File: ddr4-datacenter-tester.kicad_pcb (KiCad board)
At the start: 10 copper layers, 152.9 x 90 mm, 288 parts, among them IC1 TPS54561, IC3 TPD8S009DSMR, J1 0878311420, J10 61300311121, J3 DC_SOCKET, J4 WE_629105150521, J6 685119134923, J7 1140084168, J8 61300311121, Q2 BSS138APW, Q3 BSS138APW, Q4 BSS138APW, Q5 BSS138APW, Q6 BSS138APW, Q7 BSS138APW, Q8 BSS138APW, U10 LM3881MME_NOPB, U11 S27KL0641DABHI023, U12 TPS62823DLCT, U14 2199155-1, U15 XC7K160T-FFG676, U2 ASFLMB-100.000MHZ-XY-T, U3 S25FL128SAGNFI000, U4 TPS65296, U5 TPS62823DLCT, U6 KSZ9031RNXCA, U7 FT4232HQ, U8 SRST, U9 TPS62823DLCT, Y1 ABM8G-25.000MHZ-18-D2Y-T, Y2 ABM8G-12.000MHZ-18-D2Y-T

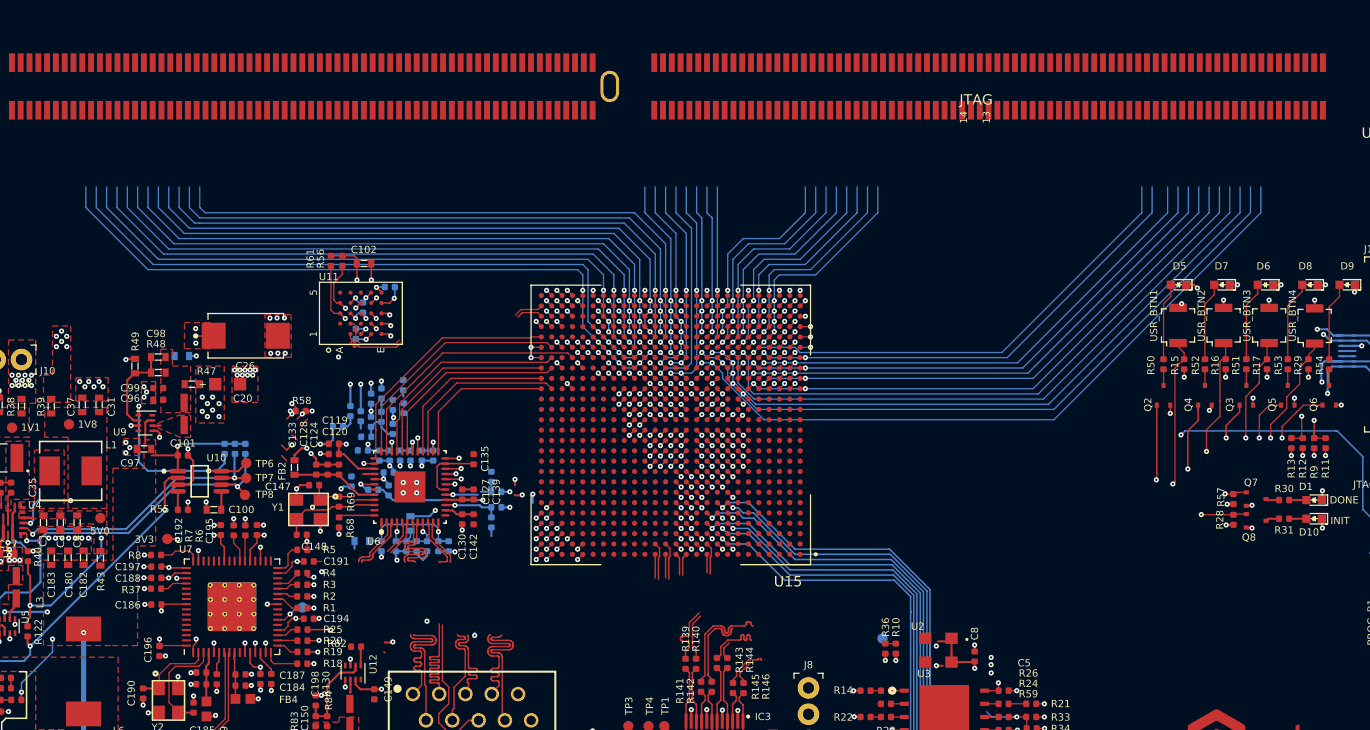
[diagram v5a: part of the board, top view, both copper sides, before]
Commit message: ADD DDR4 connection to FPGA and signals routing - WIP
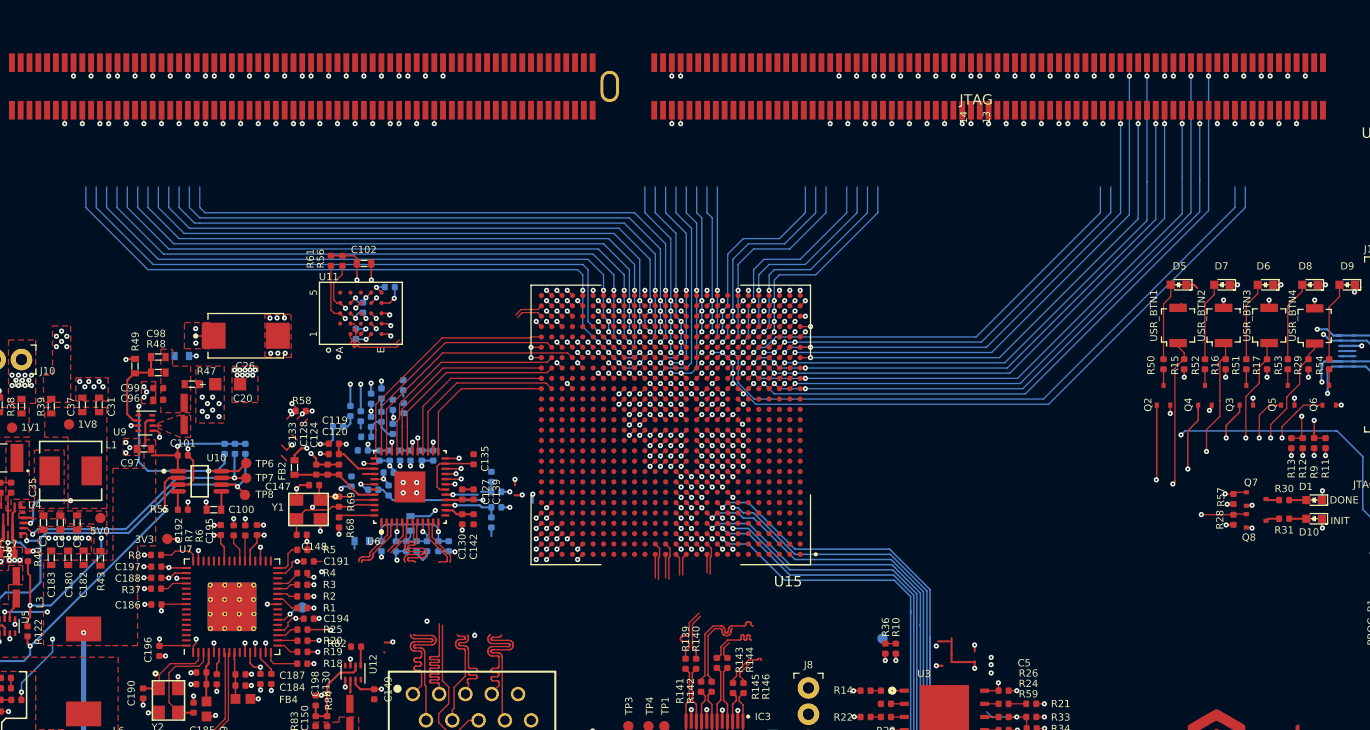
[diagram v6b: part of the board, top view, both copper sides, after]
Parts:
- removed C8: C_100n_0402_6V3, ddr4-datacenter-tester-footprints:0402-cap
- removed U2: ASFLMB-100.000MHZ-XY-T, ddr4-datacenter-tester-footprints:ASFLMB-100.000MHZ-XY-T
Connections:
- net /DDR4/12V renamed 12V
- net /DDR4/A0 renamed A0
- net /DDR4/A1 renamed A1
- net /DDR4/A10\AP renamed A10\AP
- net /DDR4/A11 renamed A11
- net /DDR4/A12\~BC renamed A12\~BC
- net /DDR4/A13 renamed A13
- net /DDR4/A17 renamed A17
- net /DDR4/A2 renamed A2
- net /DDR4/A3 renamed A3
- net /DDR4/A4 renamed A4
- net /DDR4/A5 renamed A5
- net /DDR4/A6 renamed A6
- net /DDR4/A7 renamed A7
- net /DDR4/A8 renamed A8
- net /DDR4/A9 renamed A9
- net /DDR4/BA0 renamed BA0
- net /DDR4/BA1 renamed BA1
- net /DDR4/BG0 renamed BG0
- net /DDR4/BG1 renamed BG1
- net /DDR4/CKE0 renamed CKE0
- net /DDR4/CKE1\NC renamed CKE1\NC
- net /DDR4/DQ32 renamed DQ32
- net /DDR4/DQ33 renamed DQ33
- net /DDR4/DQ34 renamed DQ34
- net /DDR4/DQ35 renamed DQ35
- net /DDR4/DQ36 renamed DQ36
- net /DDR4/DQ37 renamed DQ37
- net /DDR4/DQ38 renamed DQ38
- net /DDR4/DQ39 renamed DQ39
- net /DDR4/DQ40 renamed DQ40
- net /DDR4/DQ41 renamed DQ41
- net /DDR4/DQ42 renamed DQ42
- net /DDR4/DQ43 renamed DQ43
- net /DDR4/DQ44 renamed DQ44
- net /DDR4/DQ45 renamed DQ45
- net /DDR4/DQ46 renamed DQ46
- net /DDR4/DQ47 renamed DQ47
- net /DDR4/DQ48 renamed DQ48
- net /DDR4/DQ49 renamed DQ49
- net /DDR4/DQ50 renamed DQ50
- net /DDR4/DQ51 renamed DQ51
- net /DDR4/DQ52 renamed DQ52
- net /DDR4/DQ53 renamed DQ53
- net /DDR4/DQ54 renamed DQ54
- net /DDR4/DQ55 renamed DQ55
- net /DDR4/DQ56 renamed DQ56
- net /DDR4/DQ57 renamed DQ57
- net /DDR4/DQ58 renamed DQ58
- net /DDR4/DQ59 renamed DQ59
- net /DDR4/DQ60 renamed DQ60
- net /DDR4/DQ61 renamed DQ61
- net /DDR4/DQ62 renamed DQ62
- net /DDR4/DQ63 renamed DQ63
- net /DDR4/DQS11_C renamed DQS11_C
- net /DDR4/DQS11_T renamed DQS11_T
- net /DDR4/DQS12_C renamed DQS12_C
- net /DDR4/DQS12_T renamed DQS12_T
- net /DDR4/DQS13_C renamed DQS13_C
- net /DDR4/DQS13_T renamed DQS13_T
- net /DDR4/DQS14_C renamed DQS14_C
- net /DDR4/DQS14_T renamed DQS14_T
- net /DDR4/DQS15_C renamed DQS15_C
- net /DDR4/DQS15_T renamed DQS15_T
- net /DDR4/DQS16_C renamed DQS16_C
- net /DDR4/DQS16_T renamed DQS16_T
- net /DDR4/DQS17_C renamed DQS17_C
- net /DDR4/DQS17_T renamed DQS17_T
- net /DDR4/DQS4_C renamed DQS4_C
- net /DDR4/DQS4_T renamed DQS4_T
- net /DDR4/DQS5_C renamed DQS5_C
- net /DDR4/DQS5_T renamed DQS5_T
- net /DDR4/DQS6_C renamed DQS6_C
- net /DDR4/DQS6_T renamed DQS6_T
- net /DDR4/DQS7_C renamed DQS7_C
- net /DDR4/DQS7_T renamed DQS7_T
- net /DDR4/DQS9_C renamed DQS9_C
- net /DDR4/DQS9_T renamed DQS9_T
- net /DDR4/NC\C2 renamed NC\C2
- net /DDR4/ODT0 renamed ODT0
- net /DDR4/ODT1\NC renamed ODT1\NC
- net /DDR4/PARITY renamed PARITY
- net /DDR4/SA0 renamed SA0
- net /DDR4/SA1 renamed SA1
- net /DDR4/SA2 renamed SA2
- net /DDR4/SCL renamed SCL
- net /DDR4/SDA renamed SDA
- net /DDR4/~ACT renamed ~ACT
- net /DDR4/~ALERT renamed ~ALERT
- net /DDR4/~CAS~\A15 renamed ~CAS~\A15
- net /DDR4/~CS0 renamed ~CS0
- net /DDR4/~CS1~\NC renamed ~CS1~\NC
- net /DDR4/~CS2~\C0 renamed ~CS2~\C0
- net /DDR4/~CS3~\C1,NC renamed ~CS3~\C1,NC
- net /DDR4/~EVENT renamed ~EVENT
- net /DDR4/~RAS~\A16 renamed ~RAS~\A16
- net /DDR4/~RESET renamed ~RESET
- net /DDR4/~SAVE renamed ~SAVE
- net /DDR4/~WE~\A14 renamed ~WE~\A14
- U14 pad 10: /DDR4/DQ6 -> DQ6
- U14 pad 12: /DDR4/DQ2 -> DQ2
- U14 pad 14: /DDR4/DQ12 -> DQ12
- U14 pad 148: /DDR4/DQ5 -> DQ5
- U14 pad 150: /DDR4/DQ1 -> DQ1
- U14 pad 152: /DDR4/DQS10_C -> DQS0_C
- U14 pad 153: /DDR4/DQS10_T -> DQS0_T
- U14 pad 155: /DDR4/DQ7 -> DQ7
- U14 pad 157: /DDR4/DQ3 -> DQ3
- U14 pad 159: /DDR4/DQ13 -> DQ13
- U14 pad 16: /DDR4/DQ8 -> DQ8
- U14 pad 161: /DDR4/DQ9 -> DQ9
- U14 pad 163: /DDR4/DQS1_C -> DQS1_C
- U14 pad 164: /DDR4/DQS1_T -> DQS1_T
- U14 pad 166: /DDR4/DQ15 -> DQ15
- U14 pad 168: /DDR4/DQ11 -> DQ11
- U14 pad 170: /DDR4/DQ21 -> DQ21
- U14 pad 172: /DDR4/DQ17 -> DQ17
- U14 pad 174: /DDR4/DQS2_C -> DQS2_C
- U14 pad 175: /DDR4/DQS2_T -> DQS2_T
- U14 pad 177: /DDR4/DQ23 -> DQ23
- U14 pad 179: /DDR4/DQ19 -> DQ19
- U14 pad 18: /DDR4/DQS10_T -> DQS10_T
- U14 pad 181: /DDR4/DQ29 -> DQ29
- U14 pad 183: /DDR4/DQ25 -> DQ25
- U14 pad 185: /DDR4/DQS3_C -> DQS3_C
- U14 pad 186: /DDR4/DQS3_T -> DQS3_T
- U14 pad 188: /DDR4/DQ31 -> DQ31
- U14 pad 19: /DDR4/DQS10_C -> DQS10_C
- U14 pad 190: /DDR4/DQ27 -> DQ27
- U14 pad 192: /DDR4/CB5 -> CB5
- U14 pad 194: /DDR4/CB1 -> CB1
- U14 pad 196: /DDR4/DQS8_C -> DQS8_C
- U14 pad 197: /DDR4/DQS8_T -> DQS8_T
- U14 pad 199: /DDR4/CB7 -> CB7
- U14 pad 201: /DDR4/CB3 -> CB3
- U14 pad 21: /DDR4/DQ14 -> DQ14
- U14 pad 218: /DDR4/CK1_T -> CK1_T
- U14 pad 219: /DDR4/CK1_C -> CK1_C
- U14 pad 23: /DDR4/DQ10 -> DQ10
- U14 pad 25: /DDR4/DQ20 -> DQ20
- U14 pad 27: /DDR4/DQ16 -> DQ16
- U14 pad 3: /DDR4/DQ4 -> DQ4
- U14 pad 32: /DDR4/DQ22 -> DQ22
- U14 pad 34: /DDR4/DQ18 -> DQ18
- U14 pad 36: /DDR4/DQ28 -> DQ28
- U14 pad 38: /DDR4/DQ24 -> DQ24
- U14 pad 43: /DDR4/DQ30 -> DQ30
- U14 pad 45: /DDR4/DQ26 -> DQ26
- U14 pad 47: /DDR4/CB4 -> CB4
- U14 pad 49: /DDR4/CB0 -> CB0
- U14 pad 5: /DDR4/DQ0 -> DQ0
- U14 pad 54: /DDR4/CB6 -> CB6
- U14 pad 56: /DDR4/CB2 -> CB2
- U14 pad 74: /DDR4/CK0_T -> CK0_T
- U14 pad 75: /DDR4/CK0_C -> CK0_C
- U15 pad AA2: Net-(U15-PadAA2) -> DQ16
- U15 pad AB1: Net-(U15-PadAB1) -> DQS2_T
- U15 pad AB12: Net-(U15-PadAB12) -> CK1_C
- U15 pad AB2: Net-(U15-PadAB2) -> DQ17
- U15 pad AB7: Net-(U15-PadAB7) -> DQ28
- U15 pad AC1: Net-(U15-PadAC1) -> DQS2_C
- U15 pad AC11: Net-(U15-PadAC11) -> DQ27
- U15 pad AC12: Net-(U15-PadAC12) -> CK1_T
- U15 pad AC2: Net-(U15-PadAC2) -> DQ23
- U15 pad AC6: Net-(U15-PadAC6) -> CB3
- U15 pad AC7: Net-(U15-PadAC7) -> DQ29
- U15 pad AC8: Net-(U15-PadAC8) -> DQS3_T
- U15 pad AC9: Net-(U15-PadAC9) -> DQ31
- U15 pad AD1: Net-(U15-PadAD1) -> DQ22
- U15 pad AD10: Net-(U15-PadAD10) -> DQ26
- U15 pad AD5: Net-(U15-PadAD5) -> CB7
- U15 pad AD6: Net-(U15-PadAD6) -> CB2
- U15 pad AD8: Net-(U15-PadAD8) -> DQS3_C
- U15 pad AD9: Net-(U15-PadAD9) -> DQ30
- U15 pad AE1: Net-(U15-PadAE1) -> DQ18
- U15 pad AE12: Net-(U15-PadAE12) -> CK0_T
- U15 pad AE2: Net-(U15-PadAE2) -> DQ19
- U15 pad AE3: Net-(U15-PadAE3) -> CB5
- U15 pad AE5: Net-(U15-PadAE5) -> CB1
- U15 pad AE6: Net-(U15-PadAE6) -> CB6
- U15 pad AE7: Net-(U15-PadAE7) -> DQ24
- U15 pad AF12: Net-(U15-PadAF12) -> CK0_C
- U15 pad AF2: Net-(U15-PadAF2) -> CB4
- U15 pad AF3: Net-(U15-PadAF3) -> CB0
- U15 pad AF4: Net-(U15-PadAF4) -> DQS8_C
- U15 pad AF5: Net-(U15-PadAF5) -> DQS8_T
- U15 pad AF7: Net-(U15-PadAF7) -> DQ25
- U15 pad C15: 3V3_SYS -> Net-(U15-PadC15)
- U15 pad U2: Net-(U15-PadU2) -> DQ8
- U15 pad U4: Net-(U15-PadU4) -> DQ13
- U15 pad U5: Net-(U15-PadU5) -> DQ12
- U15 pad V11: Net-(U15-PadV11) -> DQ4
- U15 pad V2: Net-(U15-PadV2) -> DQ20
- U15 pad V6: Net-(U15-PadV6) -> DQ9
- U15 pad V7: Net-(U15-PadV7) -> DQ2
- U15 pad V8: Net-(U15-PadV8) -> DQ6
- U15 pad V9: Net-(U15-PadV9) -> DQ5
- U15 pad W1: Net-(U15-PadW1) -> DQ21
- U15 pad W10: Net-(U15-PadW10) -> DQS0_T
- U15 pad W11: Net-(U15-PadW11) -> DQ0
- U15 pad W3: Net-(U15-PadW3) -> DQ14
- U15 pad W5: Net-(U15-PadW5) -> DQS1_C
- U15 pad W6: Net-(U15-PadW6) -> DQS1_T
- U15 pad W8: Net-(U15-PadW8) -> DQ7
- U15 pad W9: Net-(U15-PadW9) -> DQS0_C
- U15 pad Y1: Net-(U15-PadY1) -> DQ15
- U15 pad Y11: Net-(U15-PadY11) -> DQ1
- U15 pad Y2: Net-(U15-PadY2) -> DQ10
- U15 pad Y3: Net-(U15-PadY3) -> DQ11
- U15 pad Y7: Net-(U15-PadY7) -> DQ3
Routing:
- net DQ4: track 0.00 -> 84.0 mm, vias 0 -> 2
- net DQ0: track 0.00 -> 81.5 mm, vias 0 -> 2
- net DQ1: track 0.00 -> 76.3 mm, vias 0 -> 2
- net DQ5: track 0.00 -> 76.1 mm, vias 0 -> 2
- net DQS0_T: track 0.00 -> 72.4 mm, vias 0 -> 2
- net DQ6: track 0.00 -> 72.2 mm, vias 0 -> 2
- net DQS0_C: track 0.00 -> 72.1 mm, vias 0 -> 2
- net DQ2: track 0.00 -> 68.7 mm, vias 0 -> 2
- net Net-(U15-PadW11): track 68.1 -> 0.00 mm, vias 1 -> 0
- net DQ7: track 0.00 -> 67.1 mm, vias 0 -> 2
- net Net-(U15-PadY11): track 67.0 -> 0.00 mm, vias 1 -> 0
- net Net-(U15-PadV11): track 65.9 -> 0.00 mm, vias 1 -> 0
- net DQ12: track 0.00 -> 65.7 mm, vias 0 -> 2
- net DQ3: track 0.00 -> 64.6 mm, vias 0 -> 2
- net Net-(U15-PadV9): track 62.0 -> 0.00 mm, vias 1 -> 0
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- added copper zone on In3_LS.Cu, net (none)
- added copper zone on In3_LS.Cu, net 1V8_SYS
- added copper zone on In3_LS.Cu, net 3V3_SYS
- added copper zone on In2_HS.Cu, net GND
- added copper zone on In3_LS.Cu, net GND
- added copper zone on In4_LS.Cu, net GND
- added copper zone on In3_LS.Cu, net VDDQ
- removed copper zone on VCC1, net (none)
- removed copper zone on VCC1, net 1V8_SYS
- removed copper zone on VCC1, net 3V3_SYS
- removed copper zone on GND2, net GND
- removed copper zone on In2.Cu, net GND
- removed copper zone on In5.Cu, net GND
- removed copper zone on VCC1, net VDDQ
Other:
- board text added: "CLK"
- board text added: "Die_1"
- board text added: "Die_2"
- board text added: "Die_3"
- board text added: "Die_4"
- board text added: "Die_5"
- board text added: "Die_6"
- board text added: "Die_7"
- board text added: "Die_8"
- board text added: "Die_9"

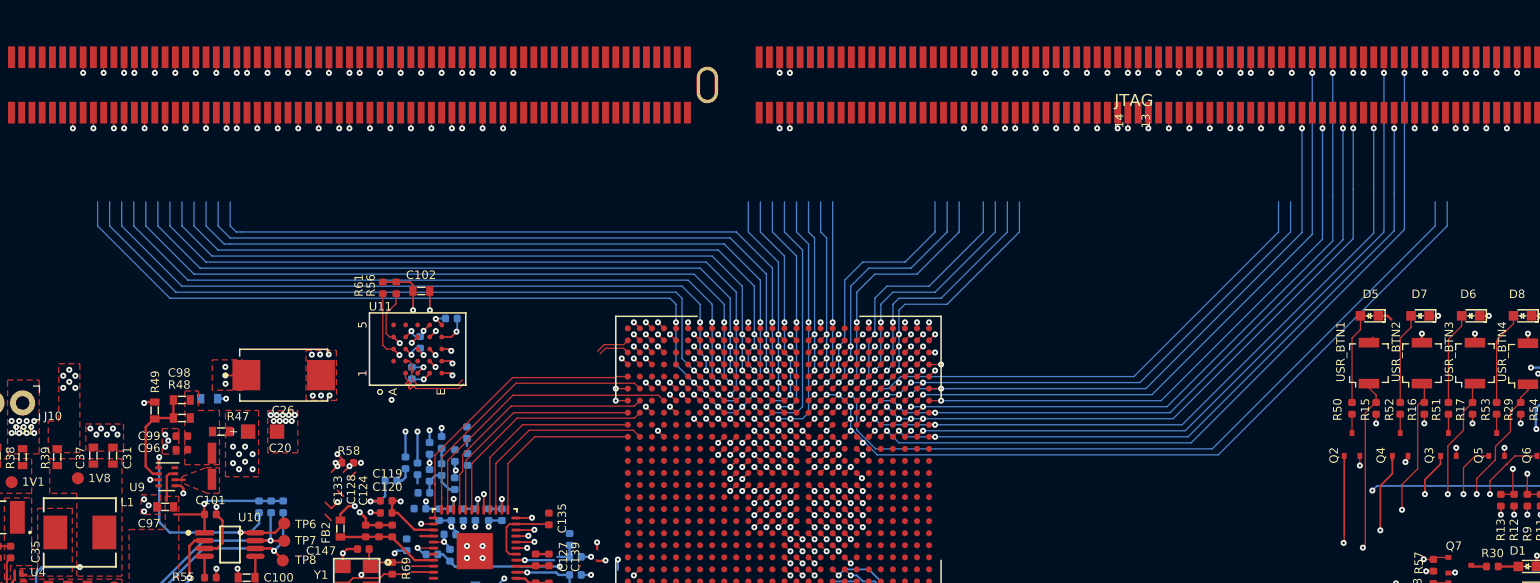
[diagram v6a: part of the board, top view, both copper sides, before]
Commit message: Connect DDR4 signals to FPGA - WIP
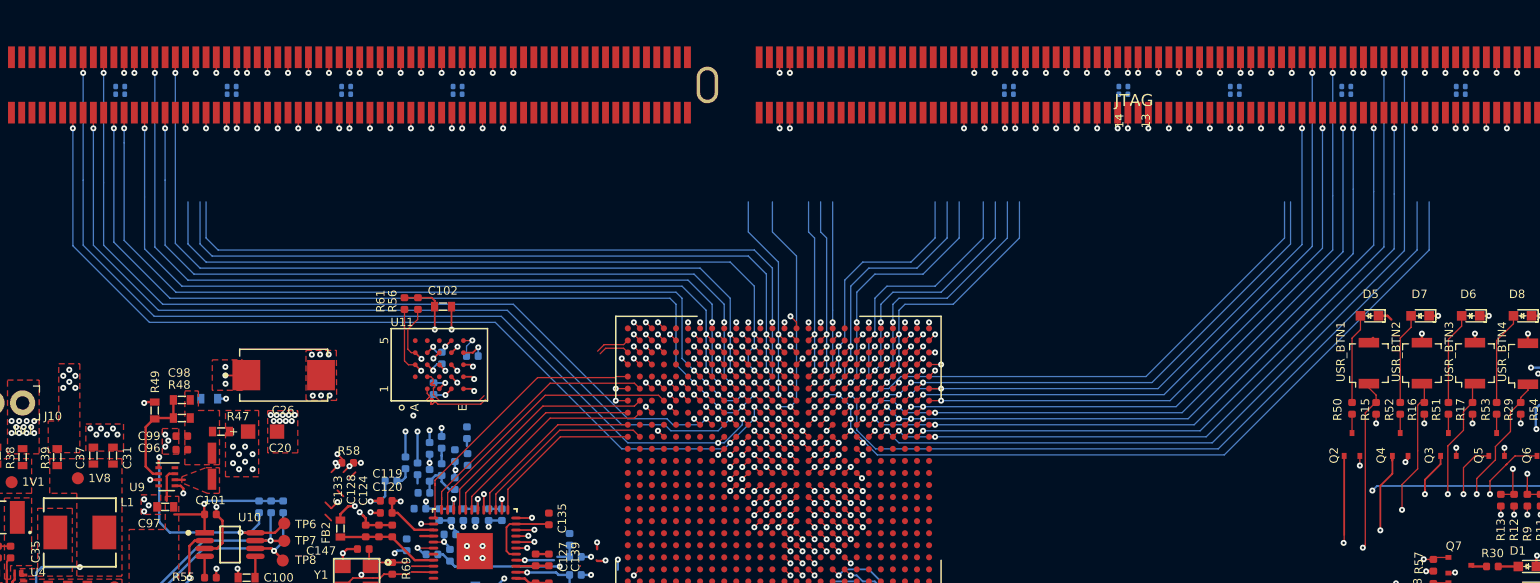
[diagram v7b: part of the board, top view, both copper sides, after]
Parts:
- added R100: R_0R_0201, antmicro-footprints:0201-res, B.Cu at (231.1, 57.8)
- added R101: R_0R_0201, antmicro-footprints:0201-res, B.Cu at (221.1, 57.8)
- added R102: R_0R_0201, antmicro-footprints:0201-res, B.Cu at (221.9, 57.8)
- added R103: R_0R_0201, antmicro-footprints:0201-res, B.Cu at (211.9, 57.8)
- added R104: R_0R_0201, antmicro-footprints:0201-res, B.Cu at (212.6, 57.8)
- added R105: R_0R_0201, antmicro-footprints:0201-res, B.Cu at (156.6, 57.8)
- added R106: R_0R_0201, antmicro-footprints:0201-res, B.Cu at (157.4, 57.8)
- added R107: R_0R_0201, antmicro-footprints:0201-res, B.Cu at (147.4, 57.8)
- added R108: R_0R_0201, antmicro-footprints:0201-res, B.Cu at (148.1, 57.8)
- added R109: R_0R_0201, antmicro-footprints:0201-res, B.Cu at (137.9, 57.8)
- added R110: R_0R_0201, antmicro-footprints:0201-res, B.Cu at (138.6, 57.8)
- added R111: R_0R_0201, antmicro-footprints:0201-res, B.Cu at (128.6, 57.8)
- added R112: R_0R_0201, antmicro-footprints:0201-res, B.Cu at (129.4, 57.8)
- added R113: R_0R_0201, antmicro-footprints:0201-res, B.Cu at (202.4, 57.8)
- added R114: R_0R_0201, antmicro-footprints:0201-res, B.Cu at (203.1, 57.8)
- added R97: R_0R_0201, antmicro-footprints:0201-res, B.Cu at (239.9, 57.8)
- added R98: R_0R_0201, antmicro-footprints:0201-res, B.Cu at (240.6, 57.8)
- added R99: R_0R_0201, antmicro-footprints:0201-res, B.Cu at (230.4, 57.8)
- moved C103 3.57 mm to (158.2, 79.9)
- moved C102 2.22 mm to (155.8, 75.8)
- moved C104 2.22 mm to (155.0, 82.6)
- moved C105 2.22 mm to (155.7, 80.0)
- moved R56 2.22 mm to (153.7, 75.5)
- moved U11 2.22 mm to (155.5, 80.6)
- moved R61 2.22 mm to (152.6, 75.5)
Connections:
- U15 pad AA15: Net-(U15-PadAA15) -> DQ53
- U15 pad AA17: Net-(U15-PadAA17) -> DQ61
- U15 pad AA18: Net-(U15-PadAA18) -> DQ56
- U15 pad AA19: Net-(U15-PadAA19) -> DQ35
- U15 pad AA20: Net-(U15-PadAA20) -> DQ52
- U15 pad AB16: Net-(U15-PadAB16) -> DQ34
- U15 pad AB17: Net-(U15-PadAB17) -> DQ60
- U15 pad AB19: Net-(U15-PadAB19) -> DQ57
- U15 pad AC16: Net-(U15-PadAC16) -> DQ32
- U15 pad AC17: Net-(U15-PadAC17) -> DQ33
- U15 pad AC18: Net-(U15-PadAC18) -> DQ38
- U15 pad AC19: Net-(U15-PadAC19) -> DQ39
- U15 pad AD15: Net-(U15-PadAD15) -> DQ36
- U15 pad AD16: Net-(U15-PadAD16) -> DQ37
- U15 pad AD18: Net-(U15-PadAD18) -> DQ47
- U15 pad AD19: Net-(U15-PadAD19) -> DQ43
- U15 pad AD20: Net-(U15-PadAD20) -> DQS4_T
- U15 pad AE15: Net-(U15-PadAE15) -> DQ44
- U15 pad AE16: Net-(U15-PadAE16) -> DQ45
- U15 pad AE17: Net-(U15-PadAE17) -> DQ41
- U15 pad AE18: Net-(U15-PadAE18) -> DQS5_T
- U15 pad AE20: Net-(U15-PadAE20) -> DQS4_C
- U15 pad AF17: Net-(U15-PadAF17) -> DQ40
- U15 pad AF18: Net-(U15-PadAF18) -> DQS5_C
- U15 pad AF19: Net-(U15-PadAF19) -> DQ46
- U15 pad AF20: Net-(U15-PadAF20) -> DQ42
- U15 pad V14: Net-(U15-PadV14) -> DQ51
- U15 pad V16: Net-(U15-PadV16) -> DQ58
- U15 pad V17: Net-(U15-PadV17) -> DQ63
- U15 pad V18: Net-(U15-PadV18) -> DQ54
- U15 pad V19: Net-(U15-PadV19) -> DQ62
- U15 pad W14: Net-(U15-PadW14) -> DQ50
- U15 pad W15: Net-(U15-PadW15) -> DQ59
- U15 pad W16: Net-(U15-PadW16) -> DQ55
- U15 pad W18: Net-(U15-PadW18) -> DQS6_T
- U15 pad W19: Net-(U15-PadW19) -> DQS6_C
- U15 pad Y15: Net-(U15-PadY15) -> DQS7_T
- U15 pad Y16: Net-(U15-PadY16) -> DQS7_C
- U15 pad Y17: Net-(U15-PadY17) -> DQ49
- U15 pad Y18: Net-(U15-PadY18) -> DQ48
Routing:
- net Net-(U15-PadV14): track 84.1 -> 0.00 mm, vias 1 -> 0
- net DQ58: track 1.30 -> 78.9 mm, vias 1 -> 2
- net DQ59: track 1.30 -> 77.3 mm, vias 1 -> 2
- net DQS7_T: track 1.30 -> 74.0 mm, vias 1 -> 2
- net DQ62: track 1.30 -> 72.7 mm, vias 1 -> 2
- net DQ50: track 1.30 -> 71.4 mm, vias 1 -> 2
- net DQ56: track 1.30 -> 71.4 mm, vias 1 -> 2
- net DQ63: track 1.30 -> 71.4 mm, vias 1 -> 2
- net DQS7_C: track 1.30 -> 71.3 mm, vias 1 -> 2
- net DQ60: track 1.30 -> 70.1 mm, vias 1 -> 2
- net Net-(U15-PadY15): track 67.2 -> 0.00 mm, vias 1 -> 0
- net DQ51: track 1.30 -> 68.2 mm, vias 1 -> 2
- net Net-(U15-PadW15): track 66.4 -> 0.00 mm, vias 1 -> 0
- net DQ61: track 1.30 -> 66.8 mm, vias 1 -> 2
- net DQ57: track 1.30 -> 65.7 mm, vias 1 -> 2
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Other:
- board text removed: "DQ_S lines- BANK32"
- board text removed: "DQ_S lines- BANK33"
- board text removed: "DQ_S lines- BANK34"
